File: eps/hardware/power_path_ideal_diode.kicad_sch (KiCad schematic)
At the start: 8 parts, among them U3 LTC4115

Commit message: add stm32 bsp and reconfigure pinout
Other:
- company: (none) -> SCRT
- title: (none) -> OSUSat CubeSat EPS
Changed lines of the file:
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@@
 	(generator_version "9.0")
 	(paper "A4")
+	(title_block
+		(title "OSUSat CubeSat EPS")
+		(date "2025-08-22")
+		(rev "1")
+		(company "SCRT")
+	)
 	(rectangle
 		(start 64.77 62.23)

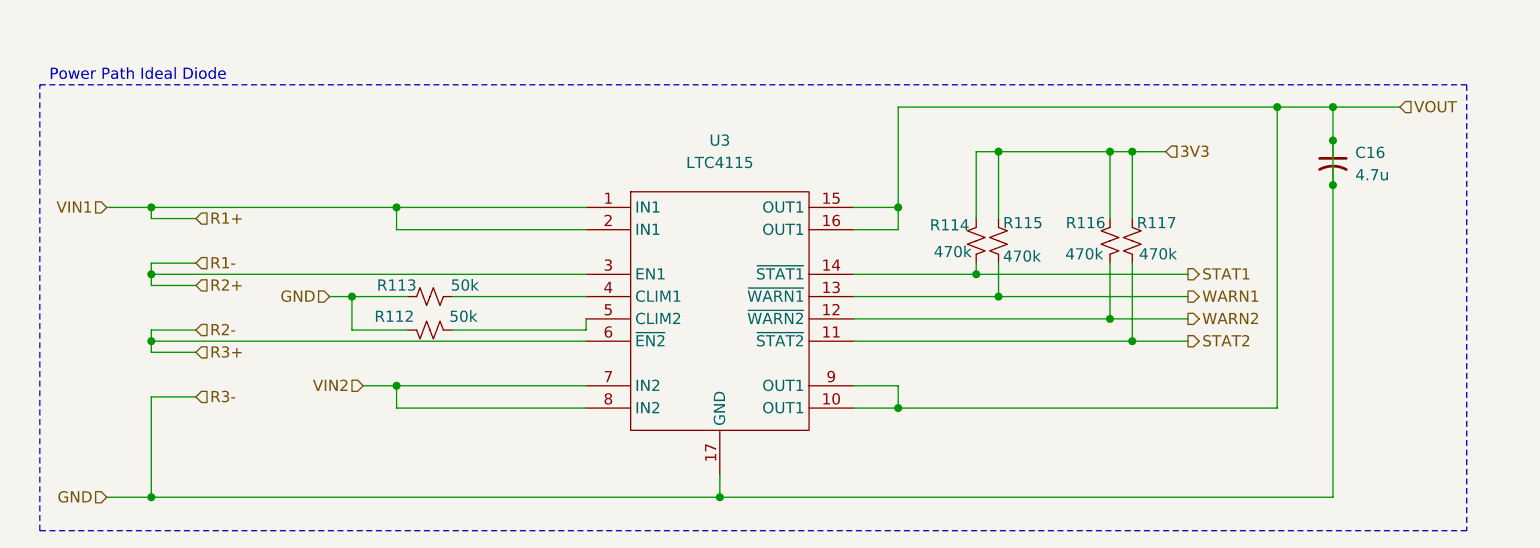
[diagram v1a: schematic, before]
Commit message: fix ERC issues
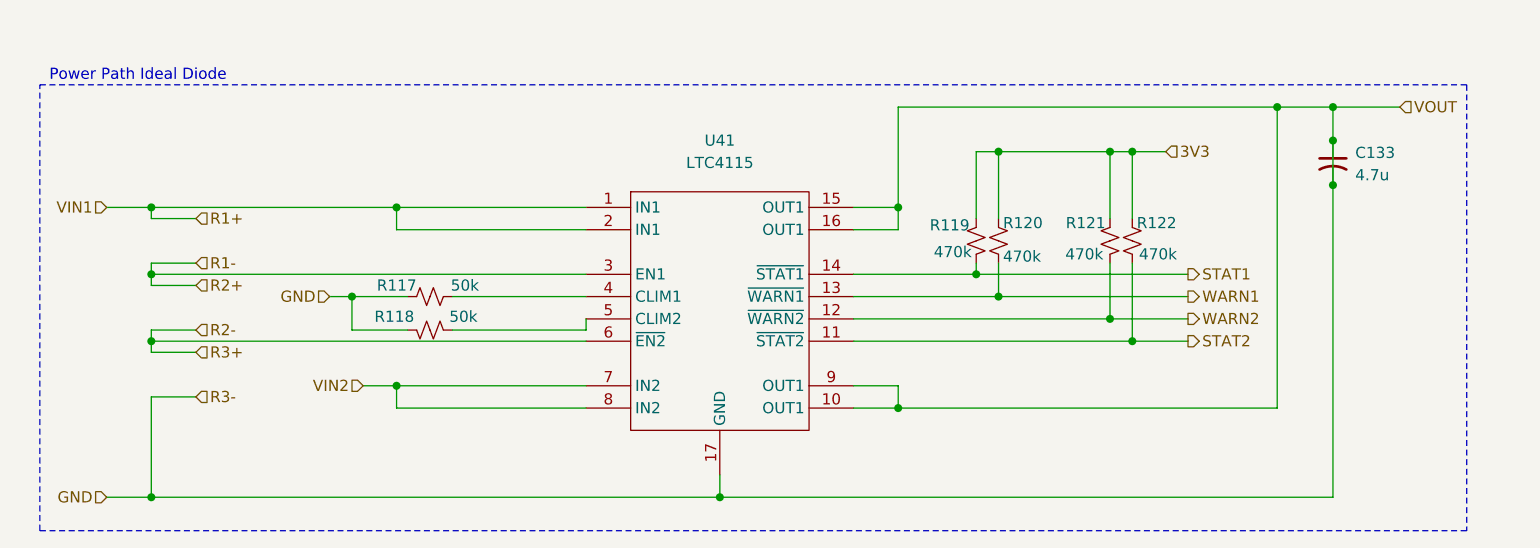
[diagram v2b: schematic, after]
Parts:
- renumbered C16 to C133, R113 to R117, R112 to R118, R114 to R119, R115 to R120, R116 to R121, R117 to R122, U3 to U41
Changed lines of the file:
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@@
 		(on_board yes)
 		(dnp no)
-		(property "Reference" "R112"
+		(property "Reference" "R118"
 			(at 105.156 88.646 90)
 			(effects
@@
 			(project "eps"
 				(path "/9e0ae2e7-d4be-41b4-8312-0d2aceea2180/ea4c86fa-6561-475a-a54d-b57bbe53e74a"
-					(reference "R125")
-					(unit 1)
-				)
-				(path "/9e0ae2e7-d4be-41b4-8312-0d2aceea2180/f7617080-eb6e-4f9f-b14e-20d6f29a9e87"
-					(reference "R112")
+					(reference "R124")
+					(unit 1)
+				)
+				(path "/9e0ae2e7-d4be-41b4-8312-0d2aceea2180/f7617080-eb6e-4f9f-b14e-20d6f29a9e87"
+					(reference "R118")
 					(unit 1)
 				)
@@
 		(on_board yes)
 		(dnp no)
-		(property "Reference" "R113"
+		(property "Reference" "R117"
 			(at 107.696 85.09 90)
 			(effects
@@
 			(project "eps"
 				(path "/9e0ae2e7-d4be-41b4-8312-0d2aceea2180/ea4c86fa-6561-475a-a54d-b57bbe53e74a"
-					(reference "R124")
-					(unit 1)
-				)
-				(path "/9e0ae2e7-d4be-41b4-8312-0d2aceea2180/f7617080-eb6e-4f9f-b14e-20d6f29a9e87"
-					(reference "R113")
+					(reference "R123")
+					(unit 1)
+				)
+				(path "/9e0ae2e7-d4be-41b4-8312-0d2aceea2180/f7617080-eb6e-4f9f-b14e-20d6f29a9e87"
+					(reference "R117")
 					(unit 1)
 				)
@@
 		(on_board yes)
 		(dnp no)
-		(property "Reference" "R117"
+		(property "Reference" "R122"
 			(at 189.738 77.978 0)
 			(effects
@@
 			(project "eps"
 				(path "/9e0ae2e7-d4be-41b4-8312-0d2aceea2180/ea4c86fa-6561-475a-a54d-b57bbe53e74a"
-					(reference "R129")
-					(unit 1)
-				)
-				(path "/9e0ae2e7-d4be-41b4-8312-0d2aceea2180/f7617080-eb6e-4f9f-b14e-20d6f29a9e87"
-					(reference "R117")
+					(reference "R128")
+					(unit 1)
+				)
+				(path "/9e0ae2e7-d4be-41b4-8312-0d2aceea2180/f7617080-eb6e-4f9f-b14e-20d6f29a9e87"
+					(reference "R122")
 					(unit 1)
 				)
@@
 		(dnp no)
 		(fields_autoplaced yes)
-		(property "Reference" "U3"
+		(property "Reference" "U41"
 			(at 142.24 68.58 0)
 			(effects
@@
 			(project "eps"
 				(path "/9e0ae2e7-d4be-41b4-8312-0d2aceea2180/ea4c86fa-6561-475a-a54d-b57bbe53e74a"
-					(reference "U5")
-					(unit 1)
-				)
-				(path "/9e0ae2e7-d4be-41b4-8312-0d2aceea2180/f7617080-eb6e-4f9f-b14e-20d6f29a9e87"
-					(reference "U3")
+					(reference "U42")
+					(unit 1)
+				)
+				(path "/9e0ae2e7-d4be-41b4-8312-0d2aceea2180/f7617080-eb6e-4f9f-b14e-20d6f29a9e87"
+					(reference "U41")
 					(unit 1)
 				)
@@
 		(on_board yes)
 		(dnp no)
-		(property "Reference" "R114"
+		(property "Reference" "R119"
 			(at 170.688 78.232 0)
 			(effects
@@
 			(project "eps"
 				(path "/9e0ae2e7-d4be-41b4-8312-0d2aceea2180/ea4c86fa-6561-475a-a54d-b57bbe53e74a"
-					(reference "R126")
-					(unit 1)
-				)
-				(path "/9e0ae2e7-d4be-41b4-8312-0d2aceea2180/f7617080-eb6e-4f9f-b14e-20d6f29a9e87"
-					(reference "R114")
+					(reference "R125")
+					(unit 1)
+				)
+				(path "/9e0ae2e7-d4be-41b4-8312-0d2aceea2180/f7617080-eb6e-4f9f-b14e-20d6f29a9e87"
+					(reference "R119")
 					(unit 1)
 				)
@@
 		(dnp no)
 		(fields_autoplaced yes)
-		(property "Reference" "C16"
+		(property "Reference" "C133"
 			(at 214.63 69.9769 0)
 			(effects
@@
 			(project "eps"
 				(path "/9e0ae2e7-d4be-41b4-8312-0d2aceea2180/ea4c86fa-6561-475a-a54d-b57bbe53e74a"
-					(reference "C23")
-					(unit 1)
-				)
-				(path "/9e0ae2e7-d4be-41b4-8312-0d2aceea2180/f7617080-eb6e-4f9f-b14e-20d6f29a9e87"
-					(reference "C16")
+					(reference "C134")
+					(unit 1)
+				)
+				(path "/9e0ae2e7-d4be-41b4-8312-0d2aceea2180/f7617080-eb6e-4f9f-b14e-20d6f29a9e87"
+					(reference "C133")
 					(unit 1)
 				)
@@
 		(on_board yes)
 		(dnp no)
-		(property "Reference" "R115"
+		(property "Reference" "R120"
 			(at 174.498 77.978 0)
 			(effects
@@
 			(project "eps"
 				(path "/9e0ae2e7-d4be-41b4-8312-0d2aceea2180/ea4c86fa-6561-475a-a54d-b57bbe53e74a"
-					(reference "R127")
-					(unit 1)
-				)
-				(path "/9e0ae2e7-d4be-41b4-8312-0d2aceea2180/f7617080-eb6e-4f9f-b14e-20d6f29a9e87"
-					(reference "R115")
+					(reference "R126")
+					(unit 1)
+				)
+				(path "/9e0ae2e7-d4be-41b4-8312-0d2aceea2180/f7617080-eb6e-4f9f-b14e-20d6f29a9e87"
+					(reference "R120")
 					(unit 1)
 				)
@@
 		(on_board yes)
 		(dnp no)
-		(property "Reference" "R116"
+		(property "Reference" "R121"
 			(at 186.182 77.978 0)
 			(effects
@@
 			(project "eps"
 				(path "/9e0ae2e7-d4be-41b4-8312-0d2aceea2180/ea4c86fa-6561-475a-a54d-b57bbe53e74a"
-					(reference "R128")
-					(unit 1)
-				)
-				(path "/9e0ae2e7-d4be-41b4-8312-0d2aceea2180/f7617080-eb6e-4f9f-b14e-20d6f29a9e87"
-					(reference "R116")
-					(unit 1)
-				)
+					(reference "R127")
+					(unit 1)
+				)
+				(path "/9e0ae2e7-d4be-41b4-8312-0d2aceea2180/f7617080-eb6e-4f9f-b14e-20d6f29a9e87"
+					(reference "R121")
+					(unit 1)
+				)

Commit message: fix all ERC errors
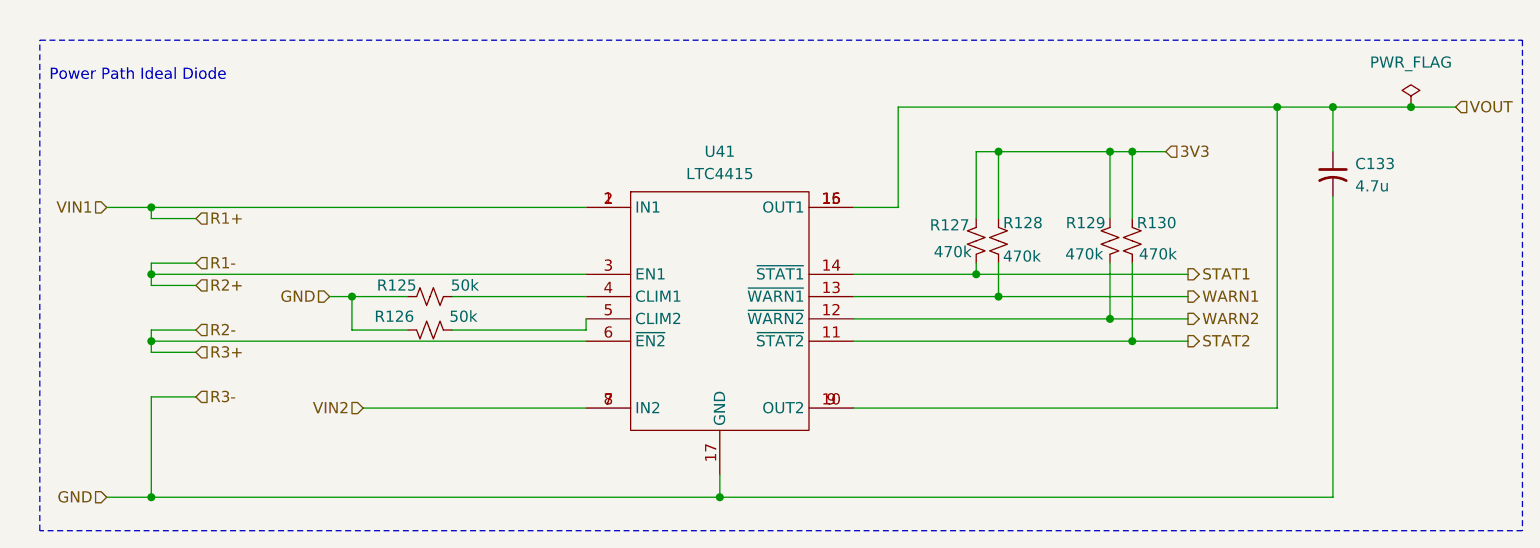
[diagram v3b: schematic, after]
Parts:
- U41: value LTC4115 -> LTC4415
- renumbered R117 to R125, R118 to R126, R119 to R127, R120 to R128, R121 to R129, R122 to R130
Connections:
- net GND: no longer C133.1, U41.10 (OUT1), U41.15 (OUT1), U41.16 (OUT1), U41.9 (OUT1)
- new net VOUT: C133.1, U41.10 (OUT2), U41.15 (OUT1), U41.16 (OUT1), U41.9 (OUT2)
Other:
- moved on the sheet: C133

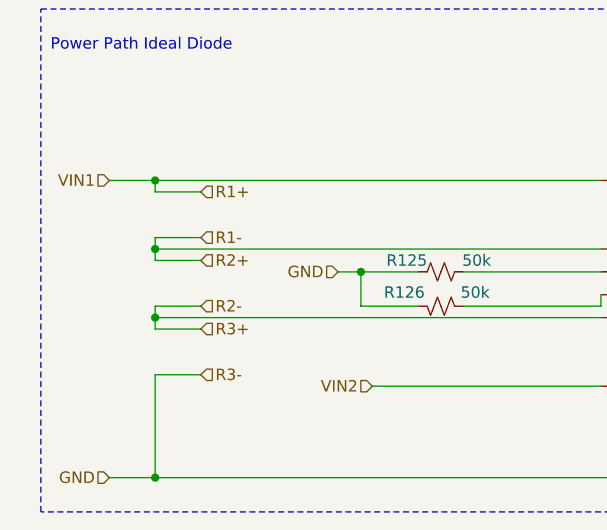
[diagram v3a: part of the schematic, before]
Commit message: fix all but one warning
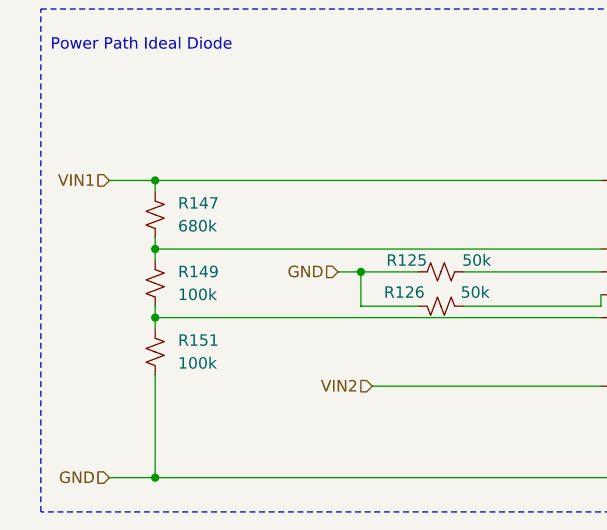
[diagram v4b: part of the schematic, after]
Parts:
- added R147: 680k, symbol Device:R_Small_US
- added R149, R151: 100k, symbol Device:R_Small_US
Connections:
- net GND: now also R151.2
- net R1+ renamed VIN1
- net VIN1: now also R147.1
- net R1-: no longer names the net of U41.3 (EN1)
- net R1-: now also R147.2, R149.1
- net R2-: no longer names the net of U41.6 (~{EN2})
- net R2-: now also R149.2, R151.1

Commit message: netlist fixes
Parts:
- renumbered R147 to R119, R149 to R120, R151 to R121, R125 to R122, R126 to R123, R127 to R124, R128 to R125, R129 to R126, R130 to R127
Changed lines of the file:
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@@
 		(on_board yes)
 		(dnp no)
-		(property "Reference" "R126"
+		(property "Reference" "R123"
 			(at 105.156 88.646 90)
 			(effects
@@
 				)
 				(path "/9e0ae2e7-d4be-41b4-8312-0d2aceea2180/f7617080-eb6e-4f9f-b14e-20d6f29a9e87"
-					(reference "R126")
+					(reference "R123")
 					(unit 1)
 				)
@@
 		(dnp no)
 		(fields_autoplaced yes)
-		(property "Reference" "R149"
+		(property "Reference" "R120"
 			(at 80.01 86.3599 0)
 			(effects
@@
 			(project ""
 				(path "/9e0ae2e7-d4be-41b4-8312-0d2aceea2180/ea4c86fa-6561-475a-a54d-b57bbe53e74a"
-					(reference "R150")
-					(unit 1)
-				)
-				(path "/9e0ae2e7-d4be-41b4-8312-0d2aceea2180/f7617080-eb6e-4f9f-b14e-20d6f29a9e87"
-					(reference "R149")
+					(reference "R129")
+					(unit 1)
+				)
+				(path "/9e0ae2e7-d4be-41b4-8312-0d2aceea2180/f7617080-eb6e-4f9f-b14e-20d6f29a9e87"
+					(reference "R120")
 					(unit 1)
 				)
@@
 		(dnp no)
 		(fields_autoplaced yes)
-		(property "Reference" "#FLG013"
+		(property "Reference" "#FLG014"
 			(at 220.98 62.865 0)
 			(effects
@@
 			(project ""
 				(path "/9e0ae2e7-d4be-41b4-8312-0d2aceea2180/ea4c86fa-6561-475a-a54d-b57bbe53e74a"
+					(reference "#FLG015")
+					(unit 1)
+				)
+				(path "/9e0ae2e7-d4be-41b4-8312-0d2aceea2180/f7617080-eb6e-4f9f-b14e-20d6f29a9e87"
 					(reference "#FLG014")
-					(unit 1)
-				)
-				(path "/9e0ae2e7-d4be-41b4-8312-0d2aceea2180/f7617080-eb6e-4f9f-b14e-20d6f29a9e87"
-					(reference "#FLG013")
 					(unit 1)
 				)
@@
 		(on_board yes)
 		(dnp no)
-		(property "Reference" "R125"
+		(property "Reference" "R122"
 			(at 107.696 85.09 90)
 			(effects
@@
 				)
 				(path "/9e0ae2e7-d4be-41b4-8312-0d2aceea2180/f7617080-eb6e-4f9f-b14e-20d6f29a9e87"
-					(reference "R125")
+					(reference "R122")
 					(unit 1)
 				)
@@
 		(on_board yes)
 		(dnp no)
-		(property "Reference" "R130"
+		(property "Reference" "R127"
 			(at 189.738 77.978 0)
 			(effects
@@
 				)
 				(path "/9e0ae2e7-d4be-41b4-8312-0d2aceea2180/f7617080-eb6e-4f9f-b14e-20d6f29a9e87"
-					(reference "R130")
+					(reference "R127")
 					(unit 1)
 				)
@@
 		(dnp no)
 		(fields_autoplaced yes)
-		(property "Reference" "R151"
+		(property "Reference" "R121"
 			(at 80.01 93.9799 0)
 			(effects
@@
 			(project "eps"
 				(path "/9e0ae2e7-d4be-41b4-8312-0d2aceea2180/ea4c86fa-6561-475a-a54d-b57bbe53e74a"
-					(reference "R152")
-					(unit 1)
-				)
-				(path "/9e0ae2e7-d4be-41b4-8312-0d2aceea2180/f7617080-eb6e-4f9f-b14e-20d6f29a9e87"
-					(reference "R151")
+					(reference "R130")
+					(unit 1)
+				)
+				(path "/9e0ae2e7-d4be-41b4-8312-0d2aceea2180/f7617080-eb6e-4f9f-b14e-20d6f29a9e87"
+					(reference "R121")
 					(unit 1)
 				)
@@
 		(on_board yes)
 		(dnp no)
-		(property "Reference" "R127"
+		(property "Reference" "R124"
 			(at 170.688 78.232 0)
 			(effects
@@
 				)
 				(path "/9e0ae2e7-d4be-41b4-8312-0d2aceea2180/f7617080-eb6e-4f9f-b14e-20d6f29a9e87"
-					(reference "R127")
+					(reference "R124")
 					(unit 1)
 				)
@@
 		(on_board yes)
 		(dnp no)
-		(property "Reference" "R128"
+		(property "Reference" "R125"
 			(at 174.498 77.978 0)
 			(effects
@@
 				)
 				(path "/9e0ae2e7-d4be-41b4-8312-0d2aceea2180/f7617080-eb6e-4f9f-b14e-20d6f29a9e87"
-					(reference "R128")
+					(reference "R125")
 					(unit 1)
 				)
@@
 		(dnp no)
 		(fields_autoplaced yes)
-		(property "Reference" "R147"
+		(property "Reference" "R119"
 			(at 80.01 78.7399 0)
 			(effects
@@
 			(project ""
 				(path "/9e0ae2e7-d4be-41b4-8312-0d2aceea2180/ea4c86fa-6561-475a-a54d-b57bbe53e74a"
-					(reference "R148")
-					(unit 1)
-				)
-				(path "/9e0ae2e7-d4be-41b4-8312-0d2aceea2180/f7617080-eb6e-4f9f-b14e-20d6f29a9e87"
-					(reference "R147")
+					(reference "R128")
+					(unit 1)
+				)
+				(path "/9e0ae2e7-d4be-41b4-8312-0d2aceea2180/f7617080-eb6e-4f9f-b14e-20d6f29a9e87"
+					(reference "R119")
 					(unit 1)
 				)
@@
 		(on_board yes)
 		(dnp no)
-		(property "Reference" "R129"
+		(property "Reference" "R126"
 			(at 186.182 77.978 0)
 			(effects
@@
 				)
 				(path "/9e0ae2e7-d4be-41b4-8312-0d2aceea2180/f7617080-eb6e-4f9f-b14e-20d6f29a9e87"
-					(reference "R129")
-					(unit 1)
-				)
+					(reference "R126")
+					(unit 1)
+				)

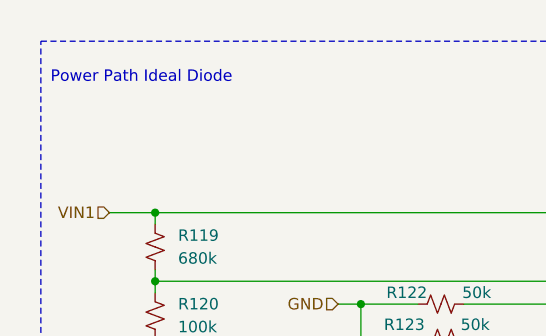
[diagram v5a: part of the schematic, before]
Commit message: start footprint assignment
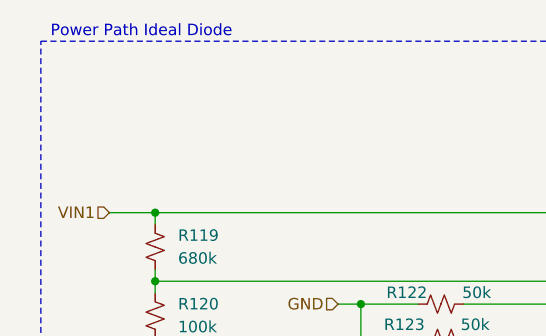
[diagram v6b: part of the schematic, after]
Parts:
- C133: footprint (none) -> Capacitor_SMD:C_0603_1608Metric
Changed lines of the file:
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@@
 	(text "Power Path Ideal Diode"
 		(exclude_from_sim no)
-		(at 75.946 61.214 0)
+		(at 75.946 56.134 0)
 		(effects
 			(font
@@
 			)
 		)
-		(property "Footprint" ""
+		(property "Footprint" "Capacitor_SMD:C_0603_1608Metric"
 			(at 212.09 72.39 0)
 			(effects

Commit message: finish footprint assignment and board setup
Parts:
- R119, R120, R121, R122, R123, R124, R125, R126, R127: footprint (none) -> Resistor_SMD:R_0603_1608Metric
- U41: footprint (none) -> Package_SO:MSOP-16-1EP_3x4.039mm_P0.5mm_EP1.651x2.845mm
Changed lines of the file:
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@@
 			)
 		)
-		(property "Footprint" ""
+		(property "Footprint" "Resistor_SMD:R_0603_1608Metric"
 			(at 109.22 90.17 0)
 			(effects
@@
 			)
 		)
-		(property "Footprint" ""
+		(property "Footprint" "Resistor_SMD:R_0603_1608Metric"
 			(at 77.47 87.63 0)
 			(effects
@@
 			)
 		)
-		(property "Footprint" ""
+		(property "Footprint" "Resistor_SMD:R_0603_1608Metric"
 			(at 109.22 86.36 0)
 			(effects
@@
 			)
 		)
-		(property "Footprint" ""
+		(property "Footprint" "Resistor_SMD:R_0603_1608Metric"
 			(at 189.23 80.01 0)
 			(effects
@@
 			)
 		)
-		(property "Footprint" ""
+		(property "Footprint" "Package_SO:MSOP-16-1EP_3x4.039mm_P0.5mm_EP1.651x2.845mm"
 			(at 142.24 71.12 0)
 			(effects
@@
 			)
 		)
-		(property "Footprint" ""
+		(property "Footprint" "Resistor_SMD:R_0603_1608Metric"
 			(at 77.47 95.25 0)
 			(effects
@@
 			)
 		)
-		(property "Footprint" ""
+		(property "Footprint" "Resistor_SMD:R_0603_1608Metric"
 			(at 171.45 80.01 0)
 			(effects
@@
 			)
 		)
-		(property "Footprint" ""
+		(property "Footprint" "Resistor_SMD:R_0603_1608Metric"
 			(at 173.99 80.01 0)
 			(effects
@@
 			)
 		)
-		(property "Footprint" ""
+		(property "Footprint" "Resistor_SMD:R_0603_1608Metric"
 			(at 77.47 80.01 0)
 			(effects
@@
 			)
 		)
-		(property "Footprint" ""
+		(property "Footprint" "Resistor_SMD:R_0603_1608Metric"
 			(at 186.69 80.01 0)
 			(effects

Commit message: schematic fixes
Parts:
- C133: footprint Capacitor_SMD:C_0603_1608Metric -> Capacitor_SMD:C_0402_1005Metric
- R119, R120, R121, R122, R123, R124, R125, R126, R127: footprint Resistor_SMD:R_0603_1608Metric -> Resistor_SMD:R_0402_1005Metric
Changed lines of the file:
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@@
 			)
 		)
-		(property "Footprint" "Resistor_SMD:R_0603_1608Metric"
+		(property "Footprint" "Resistor_SMD:R_0402_1005Metric"
 			(at 109.22 90.17 0)
 			(effects
@@
 			)
 		)
-		(property "Footprint" "Resistor_SMD:R_0603_1608Metric"
+		(property "Footprint" "Resistor_SMD:R_0402_1005Metric"
 			(at 77.47 87.63 0)
 			(effects
@@
 			)
 		)
-		(property "Footprint" "Resistor_SMD:R_0603_1608Metric"
+		(property "Footprint" "Resistor_SMD:R_0402_1005Metric"
 			(at 109.22 86.36 0)
 			(effects
@@
 			)
 		)
-		(property "Footprint" "Resistor_SMD:R_0603_1608Metric"
+		(property "Footprint" "Resistor_SMD:R_0402_1005Metric"
 			(at 189.23 80.01 0)
 			(effects
@@
 			)
 		)
-		(property "Footprint" "Resistor_SMD:R_0603_1608Metric"
+		(property "Footprint" "Resistor_SMD:R_0402_1005Metric"
 			(at 77.47 95.25 0)
 			(effects
@@
 			)
 		)
-		(property "Footprint" "Resistor_SMD:R_0603_1608Metric"
+		(property "Footprint" "Resistor_SMD:R_0402_1005Metric"
 			(at 171.45 80.01 0)
 			(effects
@@
 			)
 		)
-		(property "Footprint" "Capacitor_SMD:C_0603_1608Metric"
+		(property "Footprint" "Capacitor_SMD:C_0402_1005Metric"
 			(at 212.09 72.39 0)
 			(effects
@@
 			)
 		)
-		(property "Footprint" "Resistor_SMD:R_0603_1608Metric"
+		(property "Footprint" "Resistor_SMD:R_0402_1005Metric"
 			(at 173.99 80.01 0)
 			(effects
@@
 			)
 		)
-		(property "Footprint" "Resistor_SMD:R_0603_1608Metric"
+		(property "Footprint" "Resistor_SMD:R_0402_1005Metric"
 			(at 77.47 80.01 0)
 			(effects
@@
 			)
 		)
-		(property "Footprint" "Resistor_SMD:R_0603_1608Metric"
+		(property "Footprint" "Resistor_SMD:R_0402_1005Metric"
 			(at 186.69 80.01 0)
 			(effects
